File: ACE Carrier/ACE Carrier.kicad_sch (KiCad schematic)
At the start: 2 parts, among them J5 DF40C-34DP-0.4V_58_, J7 DF40C-34DP-0.4V_58_

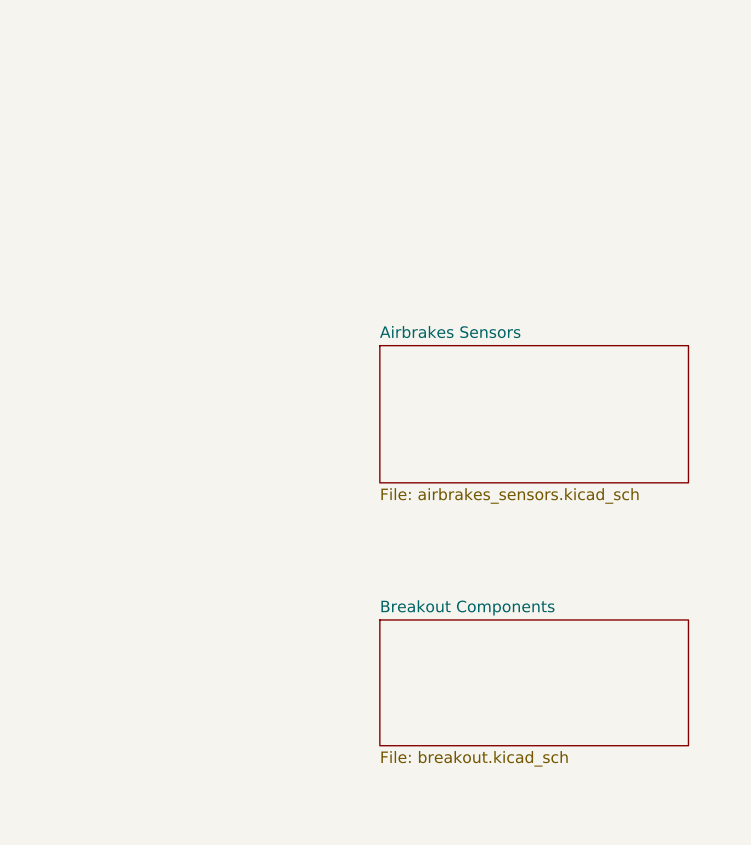
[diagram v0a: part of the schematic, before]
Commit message: added 5v power to ace carrier for pitot tube, dsub-9 pinouts, voltage divider for pitot sensor signal, changed vbus ldo on mainboard to ncp1117
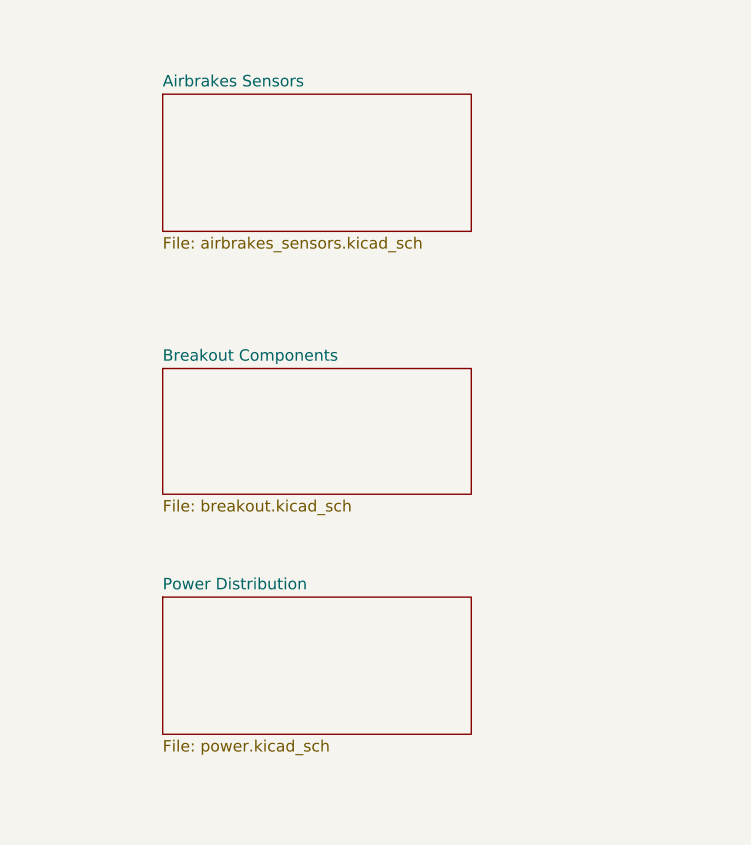
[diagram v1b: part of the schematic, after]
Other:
- added sheet Power Distribution (power.kicad_sch)
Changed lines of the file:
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@@
 	)
 	(sheet
-		(at 210.82 113.03)
+		(at 186.69 85.09)
 		(size 34.29 13.97)
 		(exclude_from_sim no)
@@
 		)
 		(property "Sheetname" "Breakout Components"
-			(at 210.82 112.3184 0)
+			(at 186.69 84.3784 0)
 			(show_name no)
 			(do_not_autoplace no)
@@
 		)
 		(property "Sheetfile" "breakout.kicad_sch"
-			(at 210.82 127.5846 0)
+			(at 186.69 99.6446 0)
 			(show_name no)
 			(do_not_autoplace no)
@@
 	)
 	(sheet
-		(at 210.82 82.55)
+		(at 186.69 54.61)
 		(size 34.29 15.24)
 		(exclude_from_sim no)
@@
 		)
 		(property "Sheetname" "Airbrakes Sensors"
-			(at 210.82 81.8384 0)
+			(at 186.69 53.8984 0)
 			(show_name no)
 			(do_not_autoplace no)
@@
 		)
 		(property "Sheetfile" "airbrakes_sensors.kicad_sch"
-			(at 210.82 98.3746 0)
+			(at 186.69 70.4346 0)
 			(show_name no)
 			(do_not_autoplace no)
@@
 				)
 			)
+		)
+	)
+	(sheet
+		(at 186.69 110.49)
+		(size 34.29 15.24)
+		(exclude_from_sim no)
+		(in_bom yes)
+		(on_board yes)
+		(dnp no)
+		(fields_autoplaced yes)
+		(stroke
+			(width 0.1524)
+			(type solid)
+		)
+		(fill
+			(color 0 0 0 0)
+		)
+		(property "Sheetname" "Power Distribution"
+			(at 186.69 109.7784 0)
+			(show_name no)
+			(do_not_autoplace no)
+			(effects
+				(font
+					(size 1.27 1.27)
+				)
+				(justify left bottom)
+			)
+		)
+		(property "Sheetfile" "power.kicad_sch"
+			(at 186.69 126.3146 0)
+			(show_name no)
+			(do_not_autoplace no)
+			(effects
+				(font
+					(size 1.27 1.27)
+				)
+				(justify left top)
+			)
+		)
+		(instances
+			(project "ACE Carrier"
+				(path "/bfe3df76-cf57-4896-b2fe-4558db46d4af"
+					(page "4")
+				)
+			)

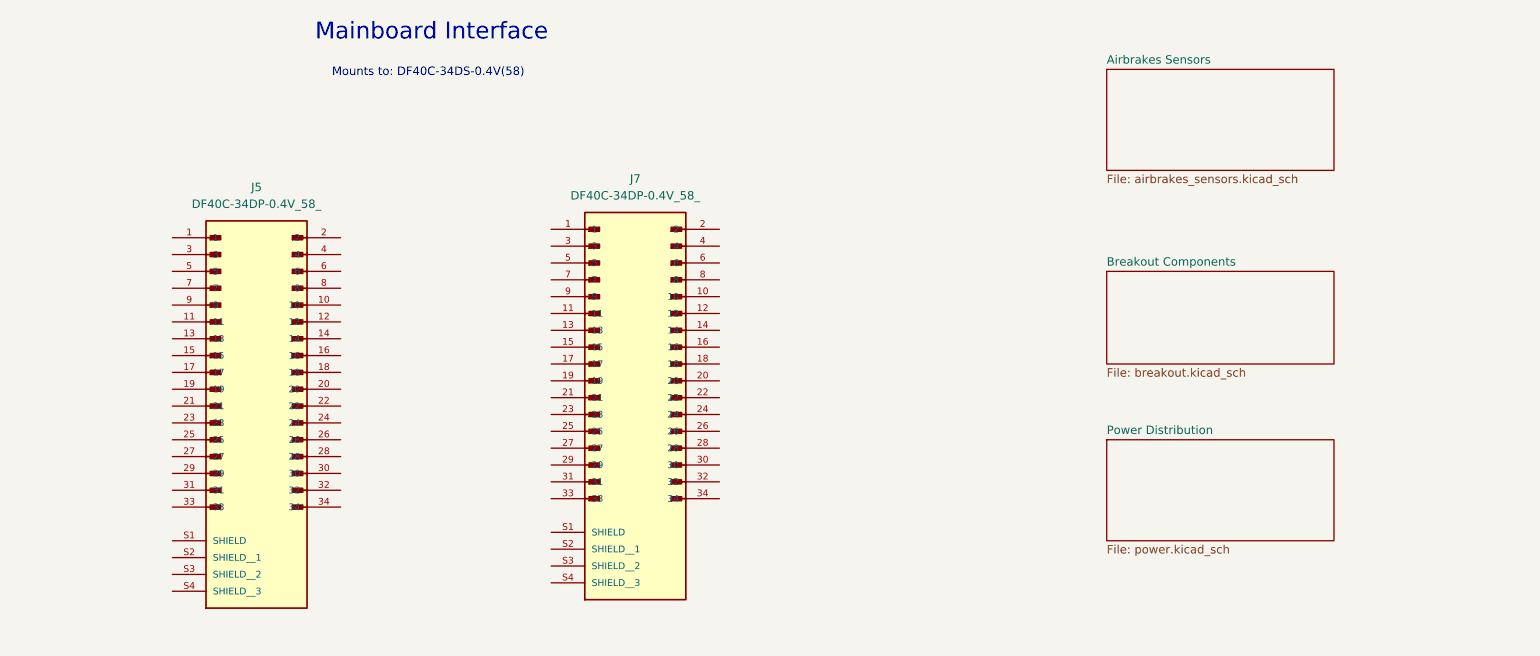
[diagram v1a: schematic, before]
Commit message: added pinouts for board interface, b3b xh servo connector and 6v buck to ace carrier
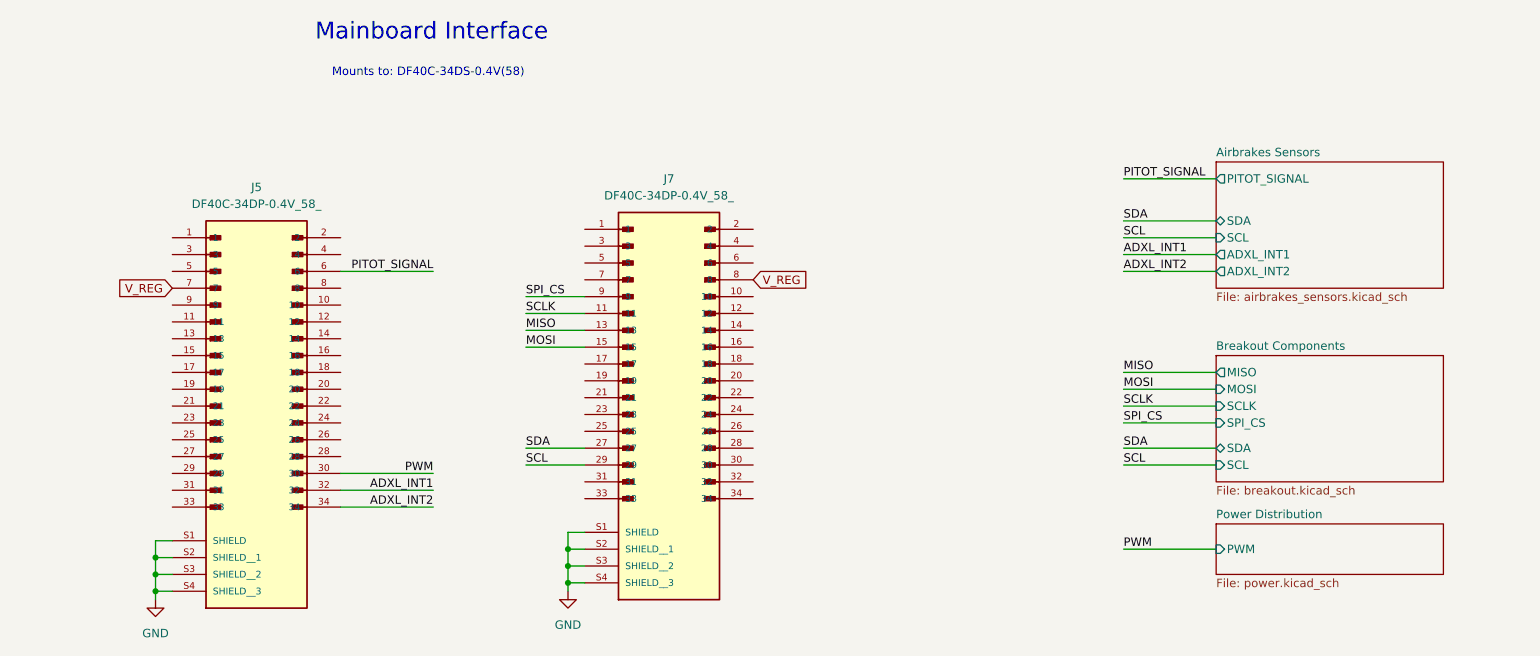
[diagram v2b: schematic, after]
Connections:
- net SCLK: now reaches J7.11
- net MISO: now reaches J7.13
- net MOSI: now reaches J7.15
- net SDA: now reaches J7.27
- net SCL: now reaches J7.29
- net V_REG: now reaches J7.8
- net V_REG: now also J5.7
- net SPI_CS: now reaches J7.9
- net GND: now reaches J7.S1 (SHIELD)
- net GND: now also J5.S1 (SHIELD), J5.S2 (SHIELD__1), J5.S3 (SHIELD__2), J5.S4 (SHIELD__3), J7.S2 (SHIELD__1), J7.S3 (SHIELD__2), J7.S4 (SHIELD__3)
- net PWM: now reaches J5.30
- net ADXL_INT1: now reaches J5.32
- net ADXL_INT2: now reaches J5.34
- net PITOT_SIGNAL: now reaches J5.6
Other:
- sheet Airbrakes Sensors ports: added ADXL_INT1, ADXL_INT2, PITOT_SIGNAL, SCL, SDA; removed none
- sheet Breakout Components ports: added MISO, MOSI, SCL, SCLK, SDA, SPI_CS; removed none
- sheet Power Distribution ports: added PWM; removed none
- moved on the sheet: J7

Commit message: H-Bridge wiring + motor ports, cleaned up carrier schematics, added MISO source terminating resistors on carriers
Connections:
- net V_REG renamed +3V3_REG
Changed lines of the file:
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@@
+	(wire
+		(pts
+			(xy 133.35 86.36) (xy 140.97 86.36)
+		)
+		(stroke
+			(width 0)
+			(type default)
+		)
+	)
 	(wire
 		(pts
@@
 		(pts
 			(xy 99.06 111.76) (xy 107.95 111.76)
+		)
+		(stroke
+			(width 0)
+			(type default)
+		)
+	)
+	(wire
+		(pts
+			(xy 38.1 87.63) (xy 45.72 87.63)
 		)
 		(stroke
@@
 		)
 	)
-	(global_label "V_REG"
-		(shape input)
-		(at 133.35 86.36 0)
-		(fields_autoplaced yes)
-		(effects
-			(font
-				(size 1.27 1.27)
-			)
-			(justify left)
-		)
-		(property "Intersheetrefs" "${INTERSHEET_REFS}"
-			(at 142.0804 86.36 0)
-			(hide yes)
+	(symbol
+		(lib_id "power:+3.3V")
+		(at 140.97 86.36 0)
+		(unit 1)
+		(body_style 1)
+		(exclude_from_sim no)
+		(in_bom yes)
+		(on_board yes)
+		(in_pos_files yes)
+		(dnp no)
+		(property "Reference" "#PWR067"
+			(at 140.97 90.17 0)
+			(hide yes)
+			(show_name no)
+			(do_not_autoplace no)
+			(effects
+				(font
+					(size 1.27 1.27)
+				)
+			)
+		)
+		(property "Value" "+3V3_REG"
+			(at 136.398 82.296 0)
 			(show_name no)
 			(do_not_autoplace no)
@@
 			)
 		)
-	)
-	(global_label "V_REG"
-		(shape input)
-		(at 45.72 87.63 180)
-		(fields_autoplaced yes)
-		(effects
-			(font
-				(size 1.27 1.27)
-			)
-			(justify right)
-		)
-		(property "Intersheetrefs" "${INTERSHEET_REFS}"
-			(at 36.9896 87.63 0)
-			(hide yes)
-			(show_name no)
-			(do_not_autoplace no)
-			(effects
-				(font
-					(size 1.27 1.27)
-				)
-				(justify right)
+		(property "Footprint" ""
+			(at 140.97 86.36 0)
+			(hide yes)
+			(show_name no)
+			(do_not_autoplace no)
+			(effects
+				(font
+					(size 1.27 1.27)
+				)
+			)
+		)
+		(property "Datasheet" ""
+			(at 140.97 86.36 0)
+			(hide yes)
+			(show_name no)
+			(do_not_autoplace no)
+			(effects
+				(font
+					(size 1.27 1.27)
+				)
+			)
+		)
+		(property "Description" "Power symbol creates a global label with name \"+3.3V\""
+			(at 140.97 86.36 0)
+			(hide yes)
+			(show_name no)
+			(do_not_autoplace no)
+			(effects
+				(font
+					(size 1.27 1.27)
+				)
+			)
+		)
+		(pin "1"
+		)
+		(instances
+			(project "ACE Carrier"
+				(path "/bfe3df76-cf57-4896-b2fe-4558db46d4af"
+					(reference "#PWR067")
+					(unit 1)
+				)
 			)
 		)
@@
 					(unit 1)
 				)
+			)
+		)
+	)
+	(symbol
+		(lib_id "power:+3.3V")
+		(at 38.1 87.63 0)
+		(unit 1)
+		(body_style 1)
+		(exclude_from_sim no)
+		(in_bom yes)
+		(on_board yes)
+		(in_pos_files yes)
+		(dnp no)
+		(property "Reference" "#PWR068"
+			(at 38.1 91.44 0)
+			(hide yes)
+			(show_name no)
+			(do_not_autoplace no)
+			(effects
+				(font
+					(size 1.27 1.27)
+				)
+			)
+		)
+		(property "Value" "+3V3_REG"
+			(at 34.29 81.534 0)
+			(show_name no)
+			(do_not_autoplace no)
+			(effects
+				(font
+					(size 1.27 1.27)
+				)
+				(justify left)
+			)
+		)
+		(property "Footprint" ""
+			(at 38.1 87.63 0)
+			(hide yes)
+			(show_name no)
+			(do_not_autoplace no)
+			(effects
+				(font
+					(size 1.27 1.27)
+				)
+			)
+		)
+		(property "Datasheet" ""
+			(at 38.1 87.63 0)
+			(hide yes)
+			(show_name no)
+			(do_not_autoplace no)
+			(effects
+				(font
+					(size 1.27 1.27)
+				)
+			)
+		)
+		(property "Description" "Power symbol creates a global label with name \"+3.3V\""
+			(at 38.1 87.63 0)
+			(hide yes)
+			(show_name no)
+			(do_not_autoplace no)
+			(effects
+				(font
+					(size 1.27 1.27)
+				)
+			)
+		)
+		(pin "1"
+		)
+		(instances
+			(project "ACE Carrier"
+				(path "/bfe3df76-cf57-4896-b2fe-4558db46d4af"
+					(reference "#PWR068")
+					(unit 1)
+				)

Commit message: update ace carrier interface pinout + initial layout
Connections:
- net +3V3_REG: now also J7.12, J7.16, J7.20, J7.24, J7.28; no longer J5.7, J7.8
- net GND: now also J5.1, J5.11, J5.25, J5.9, J7.1, J7.2, J7.32, J7.34, J7.7
- net SCL: now also J5.10; no longer J7.29
- net SDA: now also J5.8; no longer J7.27
- net +3V3: now reaches J5.3
- net +3V3: now also J5.7
- net PITOT_SIGNAL renamed PITOT_SGL
- no-connect marks 0 -> 15
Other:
- sheet Airbrakes Sensors ports: added PITOT_SGL; removed PITOT_SIGNAL
